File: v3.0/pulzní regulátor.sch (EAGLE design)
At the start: 24 parts, among them Q1 BS170, Q2 BS170, Q3 BS170, Q4 BS170

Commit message: opravena chyba pozice kurzoru v menu 1, změněn clock na externí, include knihoven eaglu.
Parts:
- R1: value (none) -> 1K5
- R2: value (none) -> 4K3
- R3: value (none) -> 5K1
- R4: value (none) -> 6K8
- R5: value (none) -> 15K
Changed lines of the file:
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@@
 <part name="GND14" library="supply1" library_urn="urn:adsk.eagle:library:371" deviceset="GND" device=""/>
 <part name="GND15" library="supply1" library_urn="urn:adsk.eagle:library:371" deviceset="GND" device=""/>
-<part name="R1" library="rcl_my" deviceset="R-EU_" device="M0805"/>
-<part name="R2" library="rcl_my" deviceset="R-EU_" device="M0805"/>
-<part name="R3" library="rcl_my" deviceset="R-EU_" device="M0805"/>
-<part name="R4" library="rcl_my" deviceset="R-EU_" device="M0805"/>
-<part name="R5" library="rcl_my" deviceset="R-EU_" device="M0805"/>
+<part name="R1" library="rcl_my" deviceset="R-EU_" device="M0805" value="1K5"/>
+<part name="R2" library="rcl_my" deviceset="R-EU_" device="M0805" value="4K3"/>
+<part name="R3" library="rcl_my" deviceset="R-EU_" device="M0805" value="5K1"/>
+<part name="R4" library="rcl_my" deviceset="R-EU_" device="M0805" value="6K8"/>
+<part name="R5" library="rcl_my" deviceset="R-EU_" device="M0805" value="15K"/>
 <part name="P+2" library="supply1" library_urn="urn:adsk.eagle:library:371" deviceset="VCC" device=""/>
 <part name="P+3" library="supply1" library_urn="urn:adsk.eagle:library:371" deviceset="VCC" device=""/>

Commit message: Úprava BUCK regulátoru z 6A na 3A, osnova dokumentace
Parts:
- removed C1, C2: (no value), rcl:CPOL-EUE5-10.5
- removed D1: MBRS130LT3, diode:MBRS130LT3
- removed U$1: AP1501TO220, regulators:AP1501TO220
- removed U$3: DTMSSDTMSS-16/0,033/6,0, induktory a trafa:DTMSSDTMSS-16/0,033/6,0
- Q1, Q2, Q3, Q4: value BS170 -> NX3008; device transistor-small-signal:BS170 -> NEXPERIA :NX3008
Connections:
- removed net N$2: D1.C, U$1.OUT, U$3.1
- net +24V: no longer C2.+, U$1.VIN
- net GND: no longer C1.-, C2.-, D1.A, U$1.GND, U$1.SD
- net N$6: no longer U$1.FB
- net VCC: no longer C1.+, U$3.2
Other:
- moved on the sheet: PAD1, PAD2, PAD3, PAD4

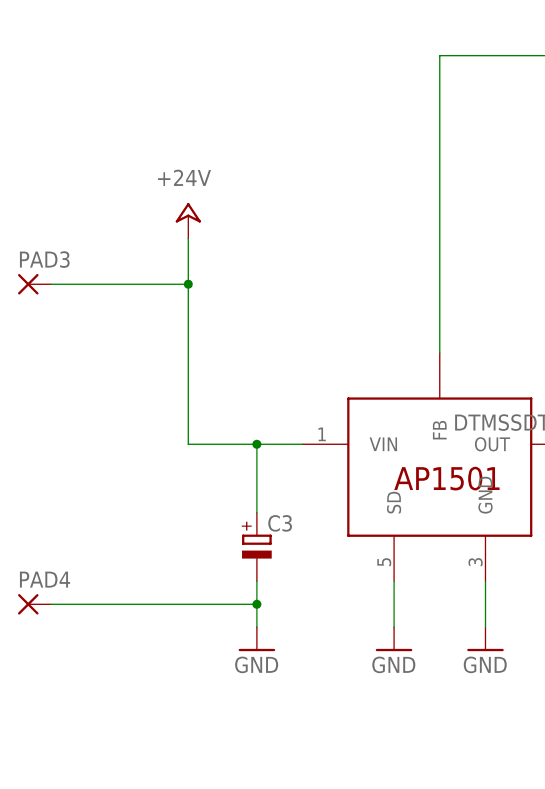
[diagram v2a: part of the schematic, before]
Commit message: regulováný zdroj pro 3A kompletní + dokumentace ovládacího panelu
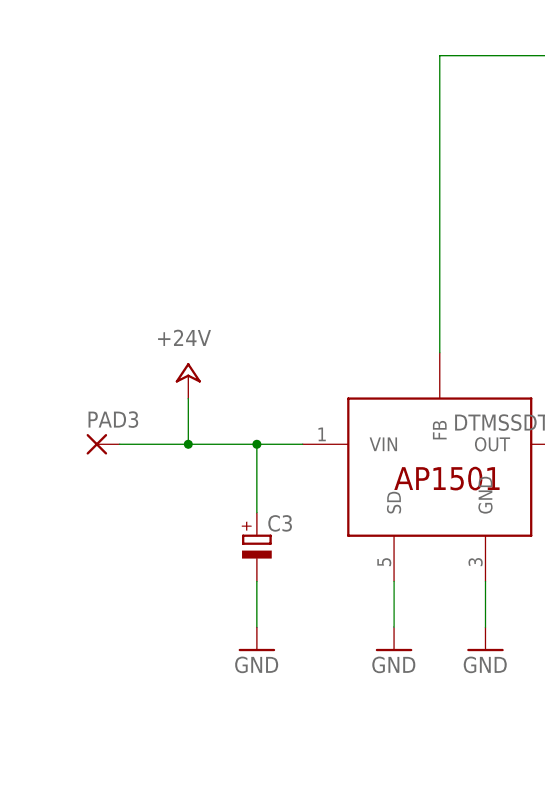
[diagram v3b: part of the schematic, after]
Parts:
- removed PAD4: (no value), wirepad:3,17/1,3
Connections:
- net GND: no longer PAD4.P
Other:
- moved on the sheet: PAD3
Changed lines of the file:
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@@
 <part name="PAD2" library="wirepad" library_urn="urn:adsk.eagle:library:412" deviceset="3,17/1,3" device="" package3d_urn="urn:adsk.eagle:package:30833/1"/>
 <part name="PAD3" library="wirepad" library_urn="urn:adsk.eagle:library:412" deviceset="3,17/1,3" device="" package3d_urn="urn:adsk.eagle:package:30833/1"/>
-<part name="PAD4" library="wirepad" library_urn="urn:adsk.eagle:library:412" deviceset="3,17/1,3" device="" package3d_urn="urn:adsk.eagle:package:30833/1"/>
 </parts>
 <sheets>
@@
 <attribute name="VALUE" x="30.48" y="-5.08" size="1.778" layer="96"/>
 </instance>
-<instance part="P+1" gate="1" x="25.4" y="45.72" smashed="yes">
-<attribute name="VALUE" x="27.94" y="50.8" size="1.778" layer="96" rot="R180"/>
+<instance part="P+1" gate="1" x="25.4" y="27.94" smashed="yes">
+<attribute name="VALUE" x="27.94" y="33.02" size="1.778" layer="96" rot="R180"/>
 </instance>
 <instance part="D2" gate="G$1" x="73.66" y="10.16" smashed="yes" rot="R90">
@@
 <attribute name="VALUE" x="102.743" y="5.842" size="1.778" layer="96" rot="R180"/>
 </instance>
-<instance part="PAD3" gate="1" x="7.62" y="38.1" smashed="yes">
-<attribute name="NAME" x="6.477" y="39.9542" size="1.778" layer="95"/>
-<attribute name="VALUE" x="6.477" y="34.798" size="1.778" layer="96"/>
-</instance>
-<instance part="PAD4" gate="1" x="7.62" y="2.54" smashed="yes">
-<attribute name="NAME" x="6.477" y="4.3942" size="1.778" layer="95"/>
-<attribute name="VALUE" x="6.477" y="-0.762" size="1.778" layer="96"/>
+<instance part="PAD3" gate="1" x="15.24" y="20.32" smashed="yes">
+<attribute name="NAME" x="14.097" y="22.1742" size="1.778" layer="95"/>
+<attribute name="VALUE" x="14.097" y="17.018" size="1.778" layer="96"/>
 </instance>
 </instances>
@@
 <wire x1="38.1" y1="20.32" x2="33.02" y2="20.32" width="0.1524" layer="91"/>
 <wire x1="33.02" y1="20.32" x2="25.4" y2="20.32" width="0.1524" layer="91"/>
-<wire x1="25.4" y1="20.32" x2="25.4" y2="38.1" width="0.1524" layer="91"/>
-<wire x1="25.4" y1="38.1" x2="25.4" y2="43.18" width="0.1524" layer="91"/>
+<wire x1="25.4" y1="20.32" x2="25.4" y2="25.4" width="0.1524" layer="91"/>
 <pinref part="C3" gate="G$1" pin="+"/>
 <wire x1="33.02" y1="12.7" x2="33.02" y2="20.32" width="0.1524" layer="91"/>
@@
 <pinref part="P+1" gate="1" pin="+24V"/>
 <pinref part="PAD3" gate="1" pin="P"/>
-<wire x1="10.16" y1="38.1" x2="25.4" y2="38.1" width="0.1524" layer="91"/>
-<junction x="25.4" y="38.1"/>
+<wire x1="17.78" y1="20.32" x2="25.4" y2="20.32" width="0.1524" layer="91"/>
+<junction x="25.4" y="20.32"/>
 </segment>
 </net>
@@
 <pinref part="GND6" gate="1" pin="GND"/>
 <pinref part="C3" gate="G$1" pin="-"/>
-<wire x1="33.02" y1="0" x2="33.02" y2="2.54" width="0.1524" layer="91"/>
-<pinref part="PAD4" gate="1" pin="P"/>
-<wire x1="33.02" y1="2.54" x2="33.02" y2="5.08" width="0.1524" layer="91"/>
-<wire x1="10.16" y1="2.54" x2="33.02" y2="2.54" width="0.1524" layer="91"/>
-<junction x="33.02" y="2.54"/>
+<wire x1="33.02" y1="0" x2="33.02" y2="5.08" width="0.1524" layer="91"/>
 </segment>
 <segment>

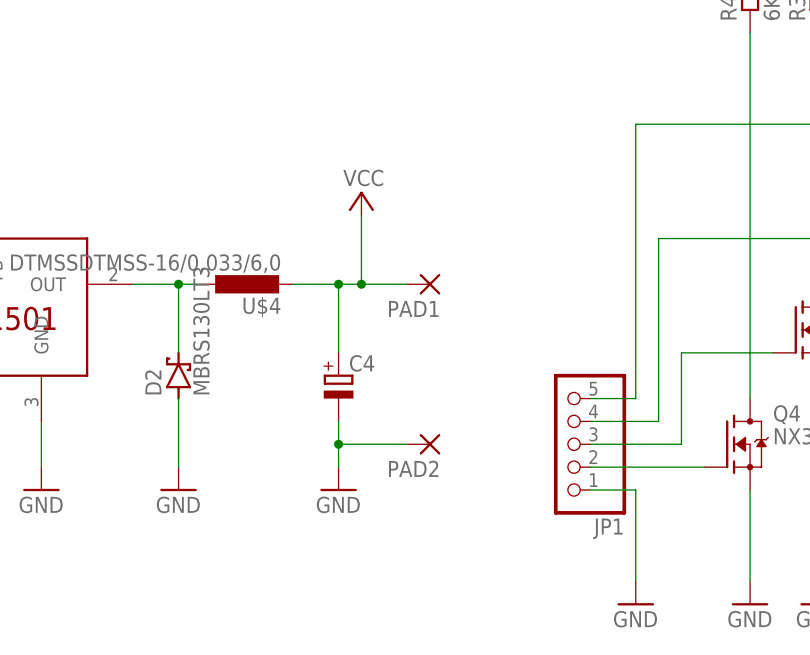
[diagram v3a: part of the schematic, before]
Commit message: přidána rozlévaná měď, rozšířena dokumentace
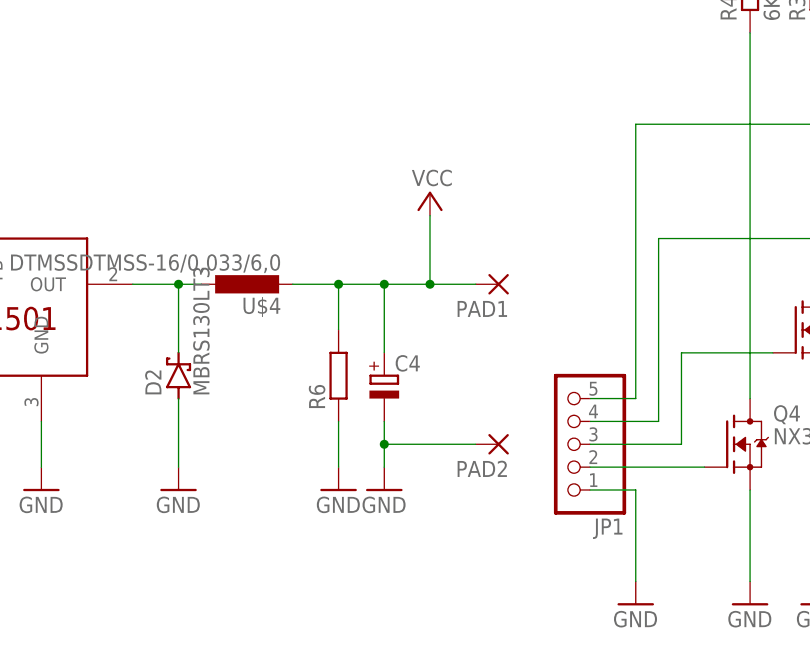
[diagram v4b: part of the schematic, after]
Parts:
- added R6: (no value), rcl:R-EU_R0805
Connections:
- net GND: now also R6.1
- net VCC: now also R6.2
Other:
- moved on the sheet: C4, PAD1, PAD2
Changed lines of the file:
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@@
 <part name="PAD2" library="wirepad" library_urn="urn:adsk.eagle:library:412" deviceset="3,17/1,3" device="" package3d_urn="urn:adsk.eagle:package:30833/1"/>
 <part name="PAD3" library="wirepad" library_urn="urn:adsk.eagle:library:412" deviceset="3,17/1,3" device="" package3d_urn="urn:adsk.eagle:package:30833/1"/>
+<part name="R6" library="rcl" library_urn="urn:adsk.eagle:library:334" deviceset="R-EU_" device="R0805" package3d_urn="urn:adsk.eagle:package:23553/2"/>
+<part name="GND3" library="supply1" library_urn="urn:adsk.eagle:library:371" deviceset="GND" device=""/>
 </parts>
 <sheets>
@@
 <attribute name="VALUE" x="34.163" y="5.5626" size="1.778" layer="96"/>
 </instance>
-<instance part="C4" gate="G$1" x="91.44" y="10.16" smashed="yes">
-<attribute name="NAME" x="92.583" y="10.6426" size="1.778" layer="95"/>
-<attribute name="VALUE" x="92.583" y="5.5626" size="1.778" layer="96"/>
-</instance>
-<instance part="GND5" gate="1" x="91.44" y="-2.54" smashed="yes">
-<attribute name="VALUE" x="88.9" y="-5.08" size="1.778" layer="96"/>
+<instance part="C4" gate="G$1" x="96.52" y="10.16" smashed="yes">
+<attribute name="NAME" x="97.663" y="10.6426" size="1.778" layer="95"/>
+<attribute name="VALUE" x="97.663" y="5.5626" size="1.778" layer="96"/>
+</instance>
+<instance part="GND5" gate="1" x="96.52" y="-2.54" smashed="yes">
+<attribute name="VALUE" x="93.98" y="-5.08" size="1.778" layer="96"/>
 </instance>
 <instance part="GND6" gate="1" x="33.02" y="-2.54" smashed="yes">
@@
 <attribute name="VALUE" x="157.48" y="86.36" size="1.778" layer="96" rot="R90"/>
 </instance>
-<instance part="P+3" gate="VCC" x="93.98" y="30.48" smashed="yes">
-<attribute name="VALUE" x="96.52" y="33.02" size="1.778" layer="96" rot="R180"/>
-</instance>
-<instance part="PAD1" gate="1" x="101.6" y="20.32" smashed="yes" rot="R180">
-<attribute name="NAME" x="102.743" y="18.4658" size="1.778" layer="95" rot="R180"/>
-<attribute name="VALUE" x="102.743" y="23.622" size="1.778" layer="96" rot="R180"/>
-</instance>
-<instance part="PAD2" gate="1" x="101.6" y="2.54" smashed="yes" rot="R180">
-<attribute name="NAME" x="102.743" y="0.6858" size="1.778" layer="95" rot="R180"/>
-<attribute name="VALUE" x="102.743" y="5.842" size="1.778" layer="96" rot="R180"/>
+<instance part="P+3" gate="VCC" x="101.6" y="30.48" smashed="yes">
+<attribute name="VALUE" x="104.14" y="33.02" size="1.778" layer="96" rot="R180"/>
+</instance>
+<instance part="PAD1" gate="1" x="109.22" y="20.32" smashed="yes" rot="R180">
+<attribute name="NAME" x="110.363" y="18.4658" size="1.778" layer="95" rot="R180"/>
+<attribute name="VALUE" x="110.363" y="23.622" size="1.778" layer="96" rot="R180"/>
+</instance>
+<instance part="PAD2" gate="1" x="109.22" y="2.54" smashed="yes" rot="R180">
+<attribute name="NAME" x="110.363" y="0.6858" size="1.778" layer="95" rot="R180"/>
+<attribute name="VALUE" x="110.363" y="5.842" size="1.778" layer="96" rot="R180"/>
 </instance>
 <instance part="PAD3" gate="1" x="15.24" y="20.32" smashed="yes">
 <attribute name="NAME" x="14.097" y="22.1742" size="1.778" layer="95"/>
 <attribute name="VALUE" x="14.097" y="17.018" size="1.778" layer="96"/>
+</instance>
+<instance part="R6" gate="G$1" x="91.44" y="10.16" smashed="yes" rot="R90">
+<attribute name="NAME" x="89.9414" y="6.35" size="1.778" layer="95" rot="R90"/>
+<attribute name="VALUE" x="94.742" y="6.35" size="1.778" layer="96" rot="R90"/>
+</instance>
+<instance part="GND3" gate="1" x="91.44" y="-2.54" smashed="yes">
+<attribute name="VALUE" x="88.9" y="-5.08" size="1.778" layer="96"/>
 </instance>
 </instances>
@@
 <pinref part="GND5" gate="1" pin="GND"/>
 <pinref part="C4" gate="G$1" pin="-"/>
-<wire x1="91.44" y1="0" x2="91.44" y2="2.54" width="0.1524" layer="91"/>
+<wire x1="96.52" y1="0" x2="96.52" y2="2.54" width="0.1524" layer="91"/>
 <pinref part="PAD2" gate="1" pin="P"/>
-<wire x1="91.44" y1="2.54" x2="91.44" y2="5.08" width="0.1524" layer="91"/>
-<wire x1="99.06" y1="2.54" x2="91.44" y2="2.54" width="0.1524" layer="91"/>
-<junction x="91.44" y="2.54"/>
+<wire x1="96.52" y1="2.54" x2="96.52" y2="5.08" width="0.1524" layer="91"/>
+<wire x1="106.68" y1="2.54" x2="96.52" y2="2.54" width="0.1524" layer="91"/>
+<junction x="96.52" y="2.54"/>
 </segment>
 <segment>
@@
 <pinref part="Q1" gate="G$1" pin="S"/>
 <wire x1="160.02" y1="-12.7" x2="160.02" y2="35.56" width="0.1524" layer="91"/>
+</segment>
+<segment>
+<pinref part="GND3" gate="1" pin="GND"/>
+<pinref part="R6" gate="G$1" pin="1"/>
+<wire x1="91.44" y1="0" x2="91.44" y2="5.08" width="0.1524" layer="91"/>
 </segment>
 </net>
@@
 <segment>
 <pinref part="U$4" gate="G$1" pin="2"/>
-<wire x1="93.98" y1="20.32" x2="91.44" y2="20.32" width="0.1524" layer="91"/>
+<wire x1="101.6" y1="20.32" x2="96.52" y2="20.32" width="0.1524" layer="91"/>
+<wire x1="96.52" y1="20.32" x2="91.44" y2="20.32" width="0.1524" layer="91"/>
+<pinref part="C4" gate="G$1" pin="+"/>
 <wire x1="91.44" y1="20.32" x2="86.36" y2="20.32" width="0.1524" layer="91"/>
-<pinref part="C4" gate="G$1" pin="+"/>
-<wire x1="91.44" y1="12.7" x2="91.44" y2="20.32" width="0.1524" layer="91"/>
+<wire x1="96.52" y1="12.7" x2="96.52" y2="20.32" width="0.1524" layer="91"/>
+<junction x="96.52" y="20.32"/>
+<pinref part="P+3" gate="VCC" pin="VCC"/>
+<wire x1="101.6" y1="20.32" x2="101.6" y2="27.94" width="0.1524" layer="91"/>
+<junction x="101.6" y="20.32"/>
+<pinref part="PAD1" gate="1" pin="P"/>
+<wire x1="106.68" y1="20.32" x2="101.6" y2="20.32" width="0.1524" layer="91"/>
+<pinref part="R6" gate="G$1" pin="2"/>
+<wire x1="91.44" y1="15.24" x2="91.44" y2="20.32" width="0.1524" layer="91"/>
 <junction x="91.44" y="20.32"/>
-<pinref part="P+3" gate="VCC" pin="VCC"/>
-<wire x1="93.98" y1="20.32" x2="93.98" y2="27.94" width="0.1524" layer="91"/>
-<junction x="93.98" y="20.32"/>
-<pinref part="PAD1" gate="1" pin="P"/>
-<wire x1="99.06" y1="20.32" x2="93.98" y2="20.32" width="0.1524" layer="91"/>
-</segment>
-<segment>
+</segment>
+<segment>
